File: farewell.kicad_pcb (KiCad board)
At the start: 2 copper layers, 211 x 72 mm, 43 parts, among them U1 0

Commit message: farewell v1 pcb
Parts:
- removed the REF** at (149.2, 50.4)
- removed the REF** at (152.3, 50.4)
- removed the REF** at (149.2, 94.7)
- removed the REF** at (152.3, 94.7)
- removed the REF** at (86.2, 51.4)
- removed the REF** at (89.3, 51.4)
- removed the REF** at (86.2, 95.7)
- removed the REF** at (89.3, 95.7)
- removed RST1: Conn_01x01, pin:Pin_D0.7mm_L6.5mm_W1.8mm_FlatFork
- added P?: CONN_1, keyboard_parts:PIN_1, F.Cu at (129.7, 40.1)
- added REF**: breakaway-mousebites, random-kb-part:breakaway-mousebites, F.Cu at (87.8, 93.7)
- added REF**: breakaway-mousebites, random-kb-part:breakaway-mousebites, F.Cu at (84.7, 93.7)
- added REF**: breakaway-mousebites, random-kb-part:breakaway-mousebites, F.Cu at (84.7, 49.4)
- added REF**: breakaway-mousebites, random-kb-part:breakaway-mousebites, F.Cu at (87.8, 49.4)
- added REF**: breakaway-mousebites, random-kb-part:breakaway-mousebites, F.Cu at (151.7, 50.4)
- added REF**: breakaway-mousebites, random-kb-part:breakaway-mousebites, F.Cu at (154.8, 50.4)
- added REF**: breakaway-mousebites, random-kb-part:breakaway-mousebites, F.Cu at (151.7, 94.7)
- added REF**: breakaway-mousebites, random-kb-part:breakaway-mousebites, F.Cu at (154.8, 94.8)
- added SW1: SW_Push, random-kb-part:PushButton_6x6mm_TH_Pretty, F.Cu at (138.8, 42.4)
- EXT1, GND_RST1, SCL1, SDA1: footprint pin:Pin_D0.7mm_L6.5mm_W1.8mm_FlatFork -> keyboard_parts:PIN_1
- MX1, MX2, MX3, MX4, MX5, MX6, MX7, MX8, MX9: footprint MX_Alps_Hybrid:MX-1U-NoLED -> farewell:MX-1U-NoLED-NoPCBMount
- moved JOY1 47.2 mm to (120.3, 53.0), turned to 0 degrees
- moved SCL1 29.6 mm to (108.0, 57.8)
- moved EXT1 27.4 mm to (108.0, 61.8)
- moved GND_RST1 25.4 mm to (132.6, 40.1)
- moved SDA1 24.5 mm to (107.9, 52.5)
- moved U1 21.8 mm to (97.8, 58.0)
- moved RE2 11.3 mm to (131.2, 49.9), turned to 0 degrees
- moved RE1 10.7 mm to (93.3, 50.0), turned to 0 degrees
- moved REF** 2.83 mm to (17.0, 106.0)
- moved REF** 2.83 mm to (17.0, 44.0)
- moved REF** 2.83 mm to (79.0, 44.0)
- moved REF** 2.83 mm to (160.0, 106.0)
- moved REF** 2.83 mm to (222.0, 106.0)
- moved REF** 2.83 mm to (222.0, 44.0)
- moved REF** 2.83 mm to (160.0, 44.0)
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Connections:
- GND_RST1 pad 1: E_G1 -> E_G2
- JOY1 pad H3: E_G1 -> E_G2
- JOY1 pad V3: E_G1 -> E_G2
- U1 pad 10: COL1 -> COL2
- U1 pad 11: COL2 -> COL1
- U1 pad 12: Net-(EXT1-Pad1) -> COL0
- U1 pad 17: ADC2 -> E2A
- U1 pad 18: ADC1 -> E2B
- U1 pad 7: E2A -> ADC1
- U1 pad 8: E2B -> Net-(EXT1-Pad1)
- U1 pad 9: COL0 -> ADC2
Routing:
- net (no net): track 0.00 -> 195.4 mm
- net E2A: track 9.38 -> 68.9 mm
- net E2B: track 15.4 -> 71.0 mm
- net Net-(SW1-Pad1): track 9.84 -> 63.6 mm, vias 0 -> 2
- net COL0: track 113.3 -> 60.7 mm
- net E_G2: track 16.0 -> 63.2 mm, vias 0 -> 1
- net VCC: track 0.00 -> 42.9 mm, vias 0 -> 2
- net COL2: track 55.2 -> 82.2 mm
- net E_G1: track 25.4 -> 7.15 mm
- net ADC2: track 0.00 -> 16.1 mm
- net ADC1: track 0.00 -> 10.9 mm
- net JOY_SW_1: track 13.7 -> 22.7 mm
- net E1B: track 11.2 -> 3.42 mm
- net E1A: track 16.3 -> 11.1 mm
- net ROW1: track 63.7 -> 58.9 mm, vias 2 -> 0
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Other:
- board size 211 x 72 mm -> 215 x 72 mm
- board text added: "GND"
- board text added: "PWM"
- board text added: "RST"
- board text added: "SCL"
- board text added: "SDA"

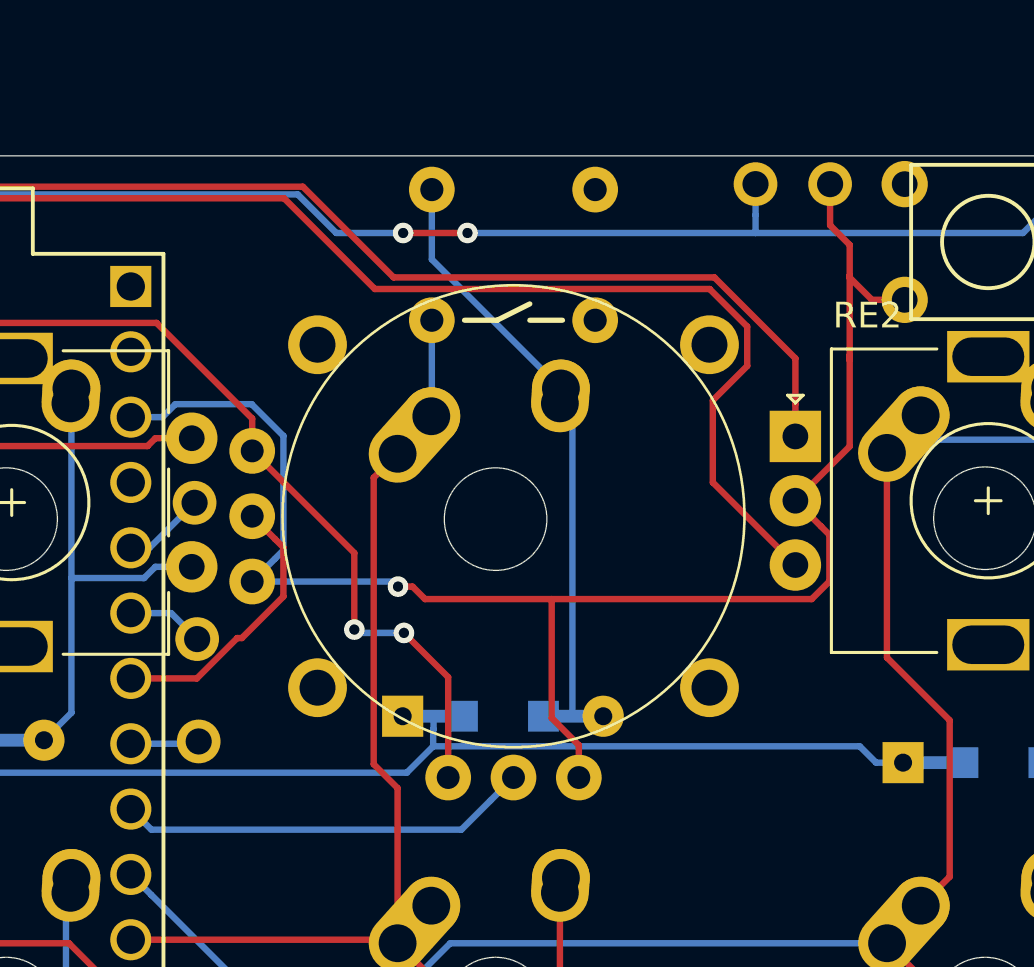
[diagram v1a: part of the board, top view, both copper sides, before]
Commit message: Fixup project path references and add submodules for required libraries
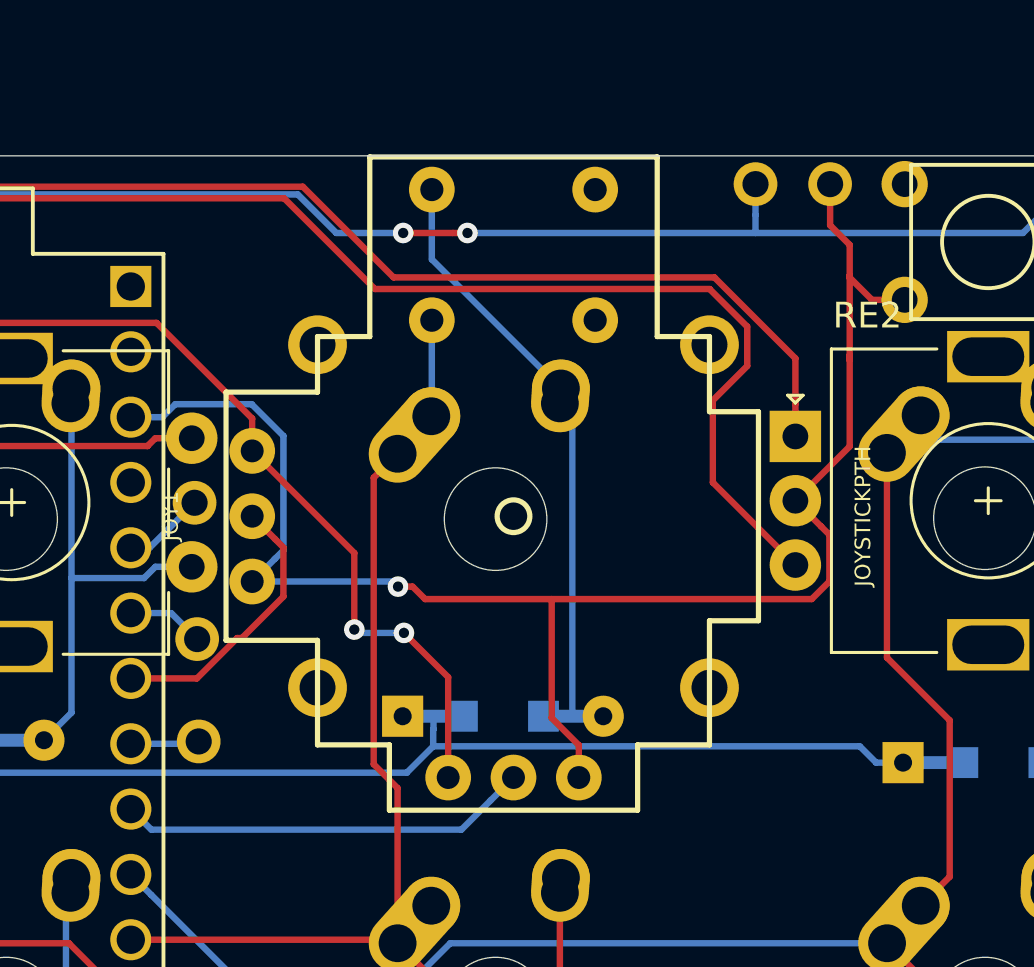
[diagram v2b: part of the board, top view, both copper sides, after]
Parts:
- JOY1: footprint sparkfun-electromech:JOYSTICK -> Switches:JOYSTICK
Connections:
- JOY1 pad B1A: JOY_SW_1 -> Net-(JOY1-PadB1A)
- JOY1 pad B2A: COL1 -> Net-(JOY1-PadB2A)
- JOY1 pad H1: VCC -> Net-(JOY1-PadH1)
- JOY1 pad H2: ADC2 -> Net-(JOY1-PadH2)
- JOY1 pad H3: E_G2 -> Net-(JOY1-PadH3)
- JOY1 pad V1: VCC -> Net-(JOY1-PadV1)
- JOY1 pad V2: ADC1 -> Net-(JOY1-PadV2)
- JOY1 pad V3: E_G2 -> Net-(JOY1-PadV3)
- MX4 pad 1: COL0 -> Net-(MX4-Pad1)
- MX5 pad 1: COL1 -> Net-(MX5-Pad1)
- MX6 pad 1: COL2 -> Net-(MX6-Pad1)
- MX7 pad 1: COL0 -> Net-(MX7-Pad1)
- MX8 pad 1: COL1 -> Net-(MX8-Pad1)
- MX9 pad 1: COL2 -> Net-(MX9-Pad1)

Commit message: [WIP] Added RGB plate
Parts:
- removed the REF** at (17.0, 106.0)
- removed the REF** at (17.0, 44.0)
- removed the REF** at (79.0, 44.0)
- removed the REF** at (84.7, 93.7)
- removed the REF** at (84.7, 49.4)
- removed the REF** at (154.8, 50.4)
- removed the REF** at (154.8, 94.8)
- removed the REF** at (79.0, 106.0)
- added REF**: breakaway-mousebites, random-kb-part:breakaway-mousebites, F.Cu at (112.5, 111.0)
- added REF**: breakaway-mousebites, random-kb-part:breakaway-mousebites, F.Cu at (112.7, 60.5)
- added REF**: breakaway-mousebites, random-kb-part:breakaway-mousebites, F.Cu at (115.3, 60.5)
- added REF**: breakaway-mousebites, random-kb-part:breakaway-mousebites, F.Cu at (115.3, 111.0)
- added REF**: MountingHole_3.2mm_M3_Pad, Mounting:MountingHole_3.2mm_M3_Pad, F.Cu at (36.5, 48.5)
- added REF**: MountingHole_3.2mm_M3_Pad, Mounting:MountingHole_3.2mm_M3_Pad, F.Cu at (108.5, 124.5)
- added REF**: MountingHole_3.2mm_M3_Pad, Mounting:MountingHole_3.2mm_M3_Pad, F.Cu at (108.5, 48.5)
- added REF**: MountingHole_3.2mm_M3_Pad, Mounting:MountingHole_3.2mm_M3_Pad, F.Cu at (36.5, 124.5)
- added RGB1: WS2812B, LED_SMD:LED_WS2812B_PLCC4_5.0x5.0mm_P3.2mm, F.Cu at (207.5, 68.8)
- added RGB2: WS2812B, LED_SMD:LED_WS2812B_PLCC4_5.0x5.0mm_P3.2mm, F.Cu at (231.5, 68.8)
- added RGB3: WS2812B, LED_SMD:LED_WS2812B_PLCC4_5.0x5.0mm_P3.2mm, F.Cu at (256.0, 64.0)
- added RGB4: WS2812B, LED_SMD:LED_WS2812B_PLCC4_5.0x5.0mm_P3.2mm, F.Cu at (255.5, 88.5)
- added RGB5: WS2812B, LED_SMD:LED_WS2812B_PLCC4_5.0x5.0mm_P3.2mm, F.Cu at (231.0, 87.5)
- added RGB6: WS2812B, LED_SMD:LED_WS2812B_PLCC4_5.0x5.0mm_P3.2mm, F.Cu at (207.5, 92.8)
- added RGB7: WS2812B, LED_SMD:LED_WS2812B_PLCC4_5.0x5.0mm_P3.2mm, F.Cu at (207.0, 112.5)
- added RGB8: WS2812B, LED_SMD:LED_WS2812B_PLCC4_5.0x5.0mm_P3.2mm, F.Cu at (232.0, 112.0)
- added RGB9: WS2812B, LED_SMD:LED_WS2812B_PLCC4_5.0x5.0mm_P3.2mm, F.Cu at (255.5, 112.0)
- added RGB_DI1: Conn_01x01, keyboard_parts:PIN_1, F.Cu at (222.5, 48.5)
- added RGB_DI_MCU1: Conn_01x01, keyboard_parts:PIN_1, F.Cu at (111.0, 36.0)
- added RGB_GND1: Conn_01x01, keyboard_parts:PIN_1, F.Cu at (241.5, 46.5)
- added RGB_GND_MCU1: Conn_01x01, keyboard_parts:PIN_1, F.Cu at (119.0, 33.0)
- added RGB_VCC1: Conn_01x01, keyboard_parts:PIN_1, F.Cu at (205.5, 49.5)
- added RGB_VCC_MCU1: Conn_01x01, keyboard_parts:PIN_1, F.Cu at (134.5, 36.5)
- SW1: moved to B.Cu
- U1: moved to F.Cu
- moved REF** 107.6 mm to (267.5, 48.5)
- moved REF** 105.2 mm to (191.3, 112.5)
- moved REF** 104.5 mm to (191.5, 62.0)
- moved REF** 49.1 mm to (267.5, 124.5)
- moved RE2 47.7 mm to (173.5, 72.0), turned to 90 degrees
- moved MX3 42.8 mm to (176.0, 112.0)
- moved D9 42.4 mm to (176.0, 121.5)
- moved SW1 42.0 mm to (179.5, 52.5)
- moved REF** 41.0 mm to (188.7, 112.5)
- moved GND_RST1 40.8 mm to (172.5, 48.5)
- moved MX6 40.6 mm to (176.0, 88.0)
- moved D8 40.2 mm to (176.0, 97.5)
- moved REF** 40.0 mm to (195.5, 124.5)
- moved D7 39.5 mm to (176.5, 76.0)
- moved EXT1 39.4 mm to (146.0, 51.0)
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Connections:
- MX4 pad 1: Net-(MX4-Pad1) -> COL0
- MX5 pad 1: Net-(MX5-Pad1) -> COL1
- MX6 pad 1: Net-(MX6-Pad1) -> COL2
- MX7 pad 1: Net-(MX7-Pad1) -> COL0
- MX8 pad 1: Net-(MX8-Pad1) -> COL1
- MX9 pad 1: Net-(MX9-Pad1) -> COL2
- U1 pad 10: COL2 -> Net-(RGB_DI_MCU1-Pad1)
- U1 pad 11: COL1 -> E1A
- U1 pad 12: COL0 -> E1B
- U1 pad 13: ROW0 -> ROW2
- U1 pad 15: ROW2 -> ROW0
- U1 pad 16: Net-(U1-Pad16) -> E2B
- U1 pad 18: E2B -> COL0
- U1 pad 19: E1A -> COL1
- U1 pad 20: E1B -> COL2
- U1 pad 23: E_G1 -> E_G2
- U1 pad 3: E_G2 -> Net-(RGB_GND_MCU1-Pad1)
- U1 pad 4: Net-(U1-Pad4) -> E_G1
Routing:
- net (no net): track 195.4 -> 1.33 mm
- net Net-(EXT1-Pad1): track 2.68 -> 49.7 mm
- net VCC: track 42.9 -> 0.00 mm, vias 2 -> 0
- net Net-(SCL1-Pad1): track 3.00 -> 39.6 mm
- net ROW0: track 74.9 -> 105.9 mm
- net E_G1: track 7.15 -> 33.8 mm
- net Net-(SDA1-Pad1): track 3.20 -> 27.4 mm
- net ROW1: track 58.9 -> 80.1 mm
- net ADC2: track 16.1 -> 0.00 mm
- net COL2: track 82.2 -> 96.8 mm
- net ADC1: track 10.9 -> 0.00 mm
- net Net-(SW1-Pad1): track 63.6 -> 52.9 mm, vias 2 -> 0
- net ROW2: track 50.7 -> 59.9 mm
- net E1B: track 3.42 -> 12.3 mm
- net E2B: track 71.0 -> 79.0 mm
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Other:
- board size 215 x 72 mm -> 239 x 84 mm

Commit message: rgb support with castellated connection
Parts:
- removed P?: CONN_1, keyboard_parts:PIN_1
- removed the REF** at (188.7, 62.0)
- removed RGB_DI1, RGB_DI_MCU1, RGB_GND1, RGB_GND_MCU1, RGB_VCC1, RGB_VCC_MCU1: Conn_01x01, keyboard_parts:PIN_1
- added ADC1_MCU1: Conn_01x01, keyboard_parts:PIN_1, F.Cu at (125.6, 106.8)
- added ADC1_SW1: Conn_01x01, keyboard_parts:PIN_1, F.Cu at (125.6, 27.7)
- added ADC2_MCU1: Conn_01x01, keyboard_parts:PIN_1, F.Cu at (160.1, 106.8)
- added ADC2_SW1: Conn_01x01, keyboard_parts:PIN_1, F.Cu at (160.1, 27.7)
- added COL0_MCU1: Conn_01x01, keyboard_parts:PIN_1, F.Cu at (134.6, 182.8)
- added COL0_SW1: Conn_01x01, keyboard_parts:PIN_1, F.Cu at (134.6, 103.7)
- added COL1_MCU1: Conn_01x01, keyboard_parts:PIN_1, F.Cu at (151.6, 182.8)
- added COL1_SW1: Conn_01x01, keyboard_parts:PIN_1, F.Cu at (151.6, 103.7)
- added COL2_MCU1: Conn_01x01, keyboard_parts:PIN_1, F.Cu at (168.6, 182.8)
- added COL2_SW1: Conn_01x01, keyboard_parts:PIN_1, F.Cu at (168.6, 103.7)
- added E1A_MCU1: Conn_01x01, keyboard_parts:PIN_1, F.Cu at (115.6, 125.8)
- added E1A_SW1: Conn_01x01, keyboard_parts:PIN_1, F.Cu at (115.6, 46.7)
- added E1B_MCU1: Conn_01x01, keyboard_parts:PIN_1, F.Cu at (115.6, 163.8)
- added E1B_SW1: Conn_01x01, keyboard_parts:PIN_1, F.Cu at (115.6, 84.7)
- added E2A_MCU1: Conn_01x01, keyboard_parts:PIN_1, F.Cu at (177.6, 106.8)
- added E2A_SW1: Conn_01x01, keyboard_parts:PIN_1, F.Cu at (177.6, 27.7)
- added E2B_MCU1: Conn_01x01, keyboard_parts:PIN_1, F.Cu at (187.6, 125.5)
- added E2B_SW1: Conn_01x01, keyboard_parts:PIN_1, F.Cu at (187.6, 46.4)
- added G_MCU1: Conn_01x01, keyboard_parts:PIN_1, F.Cu at (115.6, 144.8)
- added G_SW1: Conn_01x01, keyboard_parts:PIN_1, F.Cu at (115.6, 65.7)
- added REF**: breakaway-mousebites, random-kb-part:breakaway-mousebites, F.Cu at (96.1, 108.5)
- added REF**: breakaway-mousebites, random-kb-part:breakaway-mousebites, F.Cu at (140.5, 104.4)
- added REF**: breakaway-mousebites, random-kb-part:breakaway-mousebites, F.Cu at (140.5, 106.5)
- added RGB10: WS2812B, LED_SMD:LED_WS2812B_PLCC4_5.0x5.0mm_P3.2mm, B.Cu at (180.2, 118.0)
- added RGB11: WS2812B, LED_SMD:LED_WS2812B_PLCC4_5.0x5.0mm_P3.2mm, B.Cu at (178.8, 146.7)
- added RGB12: WS2812B, LED_SMD:LED_WS2812B_PLCC4_5.0x5.0mm_P3.2mm, B.Cu at (179.7, 174.5)
- added RGB13: WS2812B, LED_SMD:LED_WS2812B_PLCC4_5.0x5.0mm_P3.2mm, B.Cu at (151.7, 175.2)
- added RGB14: WS2812B, LED_SMD:LED_WS2812B_PLCC4_5.0x5.0mm_P3.2mm, B.Cu at (123.2, 174.5)
- added RGB15: WS2812B, LED_SMD:LED_WS2812B_PLCC4_5.0x5.0mm_P3.2mm, B.Cu at (123.2, 146.5)
- added RGB16: WS2812B, LED_SMD:LED_WS2812B_PLCC4_5.0x5.0mm_P3.2mm, B.Cu at (122.8, 118.0)
- added ROW0_MCU1: Conn_01x01, keyboard_parts:PIN_1, F.Cu at (187.6, 164.8)
- added ROW0_SW1: Conn_01x01, keyboard_parts:PIN_1, F.Cu at (187.6, 85.7)
- added ROW1_MCU1: Conn_01x01, keyboard_parts:PIN_1, F.Cu at (187.6, 151.2)
- added ROW1_SW1: Conn_01x01, keyboard_parts:PIN_1, F.Cu at (187.6, 72.1)
- added ROW2_MCU1: Conn_01x01, keyboard_parts:PIN_1, F.Cu at (187.6, 137.8)
- added ROW2_SW1: Conn_01x01, keyboard_parts:PIN_1, F.Cu at (187.6, 58.7)
- added RST1: Conn_01x01, keyboard_parts:PIN_1, F.Cu at (170.3, 106.8)
- added VCC_MCU1: Conn_01x01, keyboard_parts:PIN_1, F.Cu at (149.9, 106.8)
- added VCC_SW1: Conn_01x01, keyboard_parts:PIN_1, F.Cu at (149.9, 27.7)
- SCL1, SW1: moved to F.Cu
- moved REF** 172.8 mm to (36.1, 191.1)
- moved REF** 172.8 mm to (108.1, 191.1)
- moved REF** 172.8 mm to (36.1, 115.1)
- moved REF** 172.8 mm to (108.1, 115.1)
- moved REF** 153.8 mm to (45.5, 110.3), turned to 180 degrees
- moved REF** 143.3 mm to (45.5, 108.5), turned to 0 degrees
- moved RGB3 102.3 mm to (175.6, 127.2), turned to 90 degrees
- moved RGB8 102.2 mm to (151.7, 175.2)
- moved RGB9 101.9 mm to (175.6, 175.2)
- moved RGB5 101.8 mm to (151.6, 151.2)
- moved RGB4 101.6 mm to (175.6, 151.2)
- moved RGB7 101.2 mm to (127.6, 175.2)
- moved RGB1 99.0 mm to (127.6, 127.2), turned to 90 degrees
- moved RGB2 99.0 mm to (151.6, 127.2), turned to 90 degrees
- moved RGB6 99.0 mm to (127.6, 151.2)
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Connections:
- D1 pad 1: ROW2 -> Net-(D1-Pad1)
- D2 pad 1: ROW1 -> Net-(D2-Pad1)
- D3 pad 1: ROW0 -> Net-(D3-Pad1)
- D4 pad 1: ROW2 -> Net-(D1-Pad1)
- D5 pad 1: ROW1 -> Net-(D2-Pad1)
- D6 pad 1: ROW0 -> Net-(D3-Pad1)
- D7 pad 1: ROW2 -> Net-(D1-Pad1)
- D8 pad 1: ROW1 -> Net-(D2-Pad1)
- D9 pad 1: ROW0 -> Net-(D3-Pad1)
- GND_RST1 pad 1: E_G2 -> Net-(GND_RST1-Pad1)
- JOY1 pad B1A: Net-(JOY1-PadB1A) -> JOY_SW_1
- JOY1 pad B2A: Net-(JOY1-PadB2A) -> JOY_SW_2
- JOY1 pad H3: Net-(JOY1-PadH3) -> G_SW
- JOY1 pad V1: Net-(JOY1-PadV1) -> Net-(JOY1-PadH1)
- JOY1 pad V3: Net-(JOY1-PadV3) -> G_SW
- MX1 pad 1: COL0 -> RE1S2
- MX2 pad 1: COL1 -> JOY_SW_2
- MX3 pad 1: COL2 -> RE2S2
- MX4 pad 1: COL0 -> RE1S2
- MX5 pad 1: COL1 -> JOY_SW_2
- MX6 pad 1: COL2 -> RE2S2
- MX7 pad 1: COL0 -> RE1S2
- MX8 pad 1: COL1 -> JOY_SW_2
- MX9 pad 1: COL2 -> RE2S2
- RE1 pad A: E1A -> Net-(E1A_SW1-Pad1)
- RE1 pad B: E1B -> Net-(E1B_SW1-Pad1)
- RE1 pad C: E_G1 -> G_SW
- RE1 pad S2: COL0 -> RE1S2
- RE2 pad A: E2A -> Net-(E2A_SW1-Pad1)
- RE2 pad B: E2B -> Net-(E2B_SW1-Pad1)
- RE2 pad C: E_G2 -> G_SW
- RE2 pad S2: COL2 -> RE2S2
- RGB1 pad 1: Net-(RGB1-Pad1) -> RGB_VCC
- RGB1 pad 3: Net-(RGB1-Pad3) -> RGB_GND
- RGB1 pad 4: Net-(RGB1-Pad4) -> RGB_DI
- RGB2 pad 1: Net-(RGB1-Pad1) -> RGB_VCC
- RGB2 pad 3: Net-(RGB1-Pad3) -> RGB_GND
- RGB3 pad 1: Net-(RGB1-Pad1) -> RGB_VCC
- RGB3 pad 3: Net-(RGB1-Pad3) -> RGB_GND
- RGB4 pad 1: Net-(RGB1-Pad1) -> RGB_VCC
- RGB4 pad 3: Net-(RGB1-Pad3) -> RGB_GND
- RGB5 pad 1: Net-(RGB1-Pad1) -> RGB_VCC
- RGB5 pad 3: Net-(RGB1-Pad3) -> RGB_GND
- RGB6 pad 1: Net-(RGB1-Pad1) -> RGB_VCC
- RGB6 pad 3: Net-(RGB1-Pad3) -> RGB_GND
- RGB7 pad 1: Net-(RGB1-Pad1) -> RGB_VCC
- RGB7 pad 3: Net-(RGB1-Pad3) -> RGB_GND
- RGB8 pad 1: Net-(RGB1-Pad1) -> RGB_VCC
- RGB8 pad 3: Net-(RGB1-Pad3) -> RGB_GND
- RGB9 pad 1: Net-(RGB1-Pad1) -> RGB_VCC
- RGB9 pad 3: Net-(RGB1-Pad3) -> RGB_GND
- SW1 pad 1: Net-(SW1-Pad1) -> Net-(GND_RST1-Pad1)
- SW1 pad 2: E_G2 -> Net-(RST1-Pad1)
- U1 pad 10: Net-(RGB_DI_MCU1-Pad1) -> RGB_DI
- U1 pad 11: E1A -> Net-(E1A_MCU1-Pad1)
- U1 pad 12: E1B -> Net-(E1B_MCU1-Pad1)
- U1 pad 13: ROW2 -> Net-(ROW2_MCU1-Pad1)
- U1 pad 14: ROW1 -> Net-(ROW1_MCU1-Pad1)
- U1 pad 15: ROW0 -> Net-(ROW0_MCU1-Pad1)
- U1 pad 16: E2B -> Net-(E2B_MCU1-Pad1)
- U1 pad 17: E2A -> Net-(E2A_MCU1-Pad1)
- U1 pad 18: COL0 -> Net-(COL2_MCU1-Pad1)
- U1 pad 19: COL1 -> Net-(COL1_MCU1-Pad1)
- U1 pad 20: COL2 -> Net-(COL0_MCU1-Pad1)
- U1 pad 21: VCC -> Net-(U1-Pad21)
- U1 pad 22: Net-(SW1-Pad1) -> Net-(RST1-Pad1)
- U1 pad 23: E_G2 -> Net-(GND_RST1-Pad1)
- U1 pad 24: Net-(U1-Pad24) -> RGB_VCC
- U1 pad 3: Net-(RGB_GND_MCU1-Pad1) -> RGB_GND
- U1 pad 4: E_G1 -> Net-(U1-Pad4)
- U1 pad 7: ADC1 -> Net-(ADC1_MCU1-Pad1)
- U1 pad 9: ADC2 -> Net-(ADC2_MCU1-Pad1)
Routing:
- net RGB_GND: track 0.00 -> 318.1 mm, vias 0 -> 9
- net RGB_VCC: track 0.00 -> 295.1 mm, vias 0 -> 8
- net ROW0: track 105.9 -> 0.00 mm
- net COL2: track 96.8 -> 0.00 mm
- net RE1S2: track 0.00 -> 85.6 mm
- net Net-(COL2_MCU1-Pad1): track 0.00 -> 85.1 mm
- net G_SW: track 0.00 -> 82.9 mm
- net Net-(D3-Pad1): track 0.00 -> 81.7 mm
- net ROW1: track 80.1 -> 0.00 mm
- net Net-(ROW0_MCU1-Pad1): track 0.00 -> 79.1 mm
- net JOY_SW_2: track 0.00 -> 79.0 mm
- net E2B: track 79.0 -> 0.00 mm
- net Net-(D2-Pad1): track 0.00 -> 74.8 mm
- net Net-(COL1_MCU1-Pad1): track 0.00 -> 73.3 mm
- net RE2S2: track 0.00 -> 71.7 mm
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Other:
- board size 239 x 84 mm -> 155.5 x 171.4 mm
- board text added: "ADC1"
- board text added: "ADC2"
- board text added: "EXT. C6"
- board text added: "Gnd"
- board text added: "Reset"
- board text added: "TOP"
- board text added: "Vcc"
- board text removed: "GND"
- board text removed: "PWM"
- board text removed: "RST"

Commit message: use female header pins for connecting switch pcb to mcu pcb
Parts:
- removed ADC1_MCU1, ADC1_SW1, ADC2_MCU1, ADC2_SW1, COL0_MCU1, COL0_SW1, COL1_MCU1, COL1_SW1, COL2_MCU1, COL2_SW1, E1A_MCU1, E1A_SW1, E1B_MCU1, E1B_SW1, E2A_MCU1, E2A_SW1, E2B_MCU1, E2B_SW1, G_MCU1, G_SW1, ROW0_MCU1, ROW0_SW1, ROW1_MCU1, ROW1_SW1, ROW2_MCU1, ROW2_SW1, VCC_MCU1, VCC_SW1: Conn_01x01, keyboard_parts:PIN_1
- added J1: Conn_01x08, farewell_pcb:keebio_Header-8-Pin-ZigZag, F.Cu at (119.0, 124.1)
- added J2: Conn_01x08, farewell_pcb:keebio_Header-8-Pin-ZigZag, F.Cu at (119.0, 45.0)
- added J3: Conn_01x06, farewell_pcb:keebio_Header-6-Pin-ZigZag, F.Cu at (184.3, 127.8)
- added J4: Conn_01x06, farewell_pcb:keebio_Header-6-Pin-ZigZag, F.Cu at (184.3, 48.7)
- U1: footprint promicro:ProMicro -> farewell_pcb:keebio_ArduinoProMicro-ZigZag
- moved RST1 8.60 mm to (161.8, 108.1)
- moved GND_RST1 6.77 mm to (159.3, 108.1)
- moved EXT1 2.11 mm to (120.4, 110.9)
- moved SCL1 1.98 mm to (122.9, 110.8)
- moved SDA1 1.84 mm to (125.4, 110.8)
- moved U1 0.28 mm to (139.3, 123.9)
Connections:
- net G_SW renamed GND_SW
- net JOY_SW_2 renamed COL1_SW
- net Net-(D1-Pad1) renamed ROW2_SW
- net Net-(D2-Pad1) renamed ROW1_SW
- net Net-(D3-Pad1) renamed ROW0_SW
- net Net-(JOY1-PadH1) renamed VCC_SW
- net RE1S2 renamed COL0_SW
- net RE2S2 renamed COL2_SW
- net RGB_GND renamed GND_MCU
- JOY1 pad H2: Net-(ADC2_SW1-Pad1) -> ADC2_SW
- JOY1 pad V2: Net-(ADC1_SW1-Pad1) -> ADC1_SW
- RE1 pad A: Net-(E1A_SW1-Pad1) -> E1A_SW
- RE1 pad B: Net-(E1B_SW1-Pad1) -> E1B_SW
- RE2 pad A: Net-(E2A_SW1-Pad1) -> E2A_SW
- RE2 pad B: Net-(E2B_SW1-Pad1) -> E2B_SW
- U1 pad 11: Net-(E1A_MCU1-Pad1) -> E1A_MCU
- U1 pad 12: Net-(E1B_MCU1-Pad1) -> E1B_MCU
- U1 pad 13: Net-(ROW2_MCU1-Pad1) -> ROW0_MCU
- U1 pad 14: Net-(ROW1_MCU1-Pad1) -> ROW1_MCU
- U1 pad 15: Net-(ROW0_MCU1-Pad1) -> ROW2_MCU
- U1 pad 16: Net-(E2B_MCU1-Pad1) -> E2B_MCU
- U1 pad 17: Net-(E2A_MCU1-Pad1) -> E2A_MCU
- U1 pad 18: Net-(COL2_MCU1-Pad1) -> COL2_MCU
- U1 pad 19: Net-(COL1_MCU1-Pad1) -> COL1_MCU
- U1 pad 20: Net-(COL0_MCU1-Pad1) -> COL0_MCU
- U1 pad 21: Net-(U1-Pad21) -> VCC_MCU
- U1 pad 7: Net-(ADC1_MCU1-Pad1) -> ADC1_MCU
- U1 pad 9: Net-(ADC2_MCU1-Pad1) -> ADC2_MCU
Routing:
- net Net-(COL2_MCU1-Pad1): track 85.1 -> 0.00 mm
- net Net-(ROW0_MCU1-Pad1): track 79.1 -> 0.00 mm
- net Net-(COL1_MCU1-Pad1): track 73.3 -> 0.00 mm
- net Net-(COL0_MCU1-Pad1): track 70.4 -> 0.00 mm
- net Net-(ROW1_MCU1-Pad1): track 61.3 -> 0.00 mm
- net Net-(E2B_MCU1-Pad1): track 56.4 -> 0.00 mm
- net Net-(ADC2_MCU1-Pad1): track 49.2 -> 0.00 mm
- net Net-(E2A_MCU1-Pad1): track 44.2 -> 0.00 mm
- net COL2_MCU: track 0.00 -> 43.8 mm
- net E2A_MCU: track 0.00 -> 42.0 mm
- net Net-(ROW2_MCU1-Pad1): track 41.7 -> 0.00 mm
- net Net-(E1B_MCU1-Pad1): track 39.2 -> 0.00 mm
- net Net-(E1B_SW1-Pad1): track 39.0 -> 0.00 mm
- net E2B_MCU: track 0.00 -> 38.7 mm
- net ROW0_MCU: track 0.00 -> 38.4 mm
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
